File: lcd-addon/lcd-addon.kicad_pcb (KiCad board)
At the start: 2 copper layers, 39.4 x 26.9 mm, 8 parts, among them J1 Conn_01x02_Male, J2 Conn_01x07_Male, J4 Conn_01x10, J5 Conn_01x01_Male, J6 Conn_01x02_Male, J8 Conn_01x02_Male

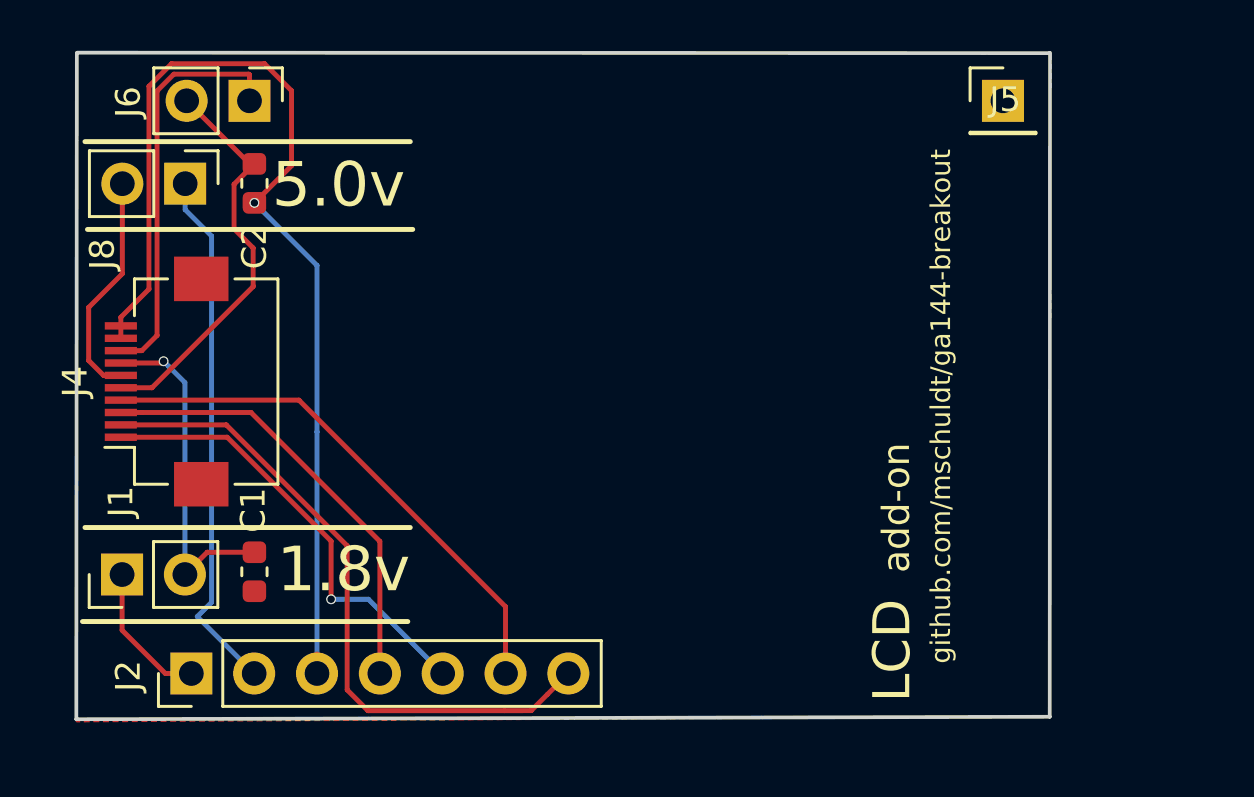
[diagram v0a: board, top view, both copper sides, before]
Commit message: lcd-addon: extend board length
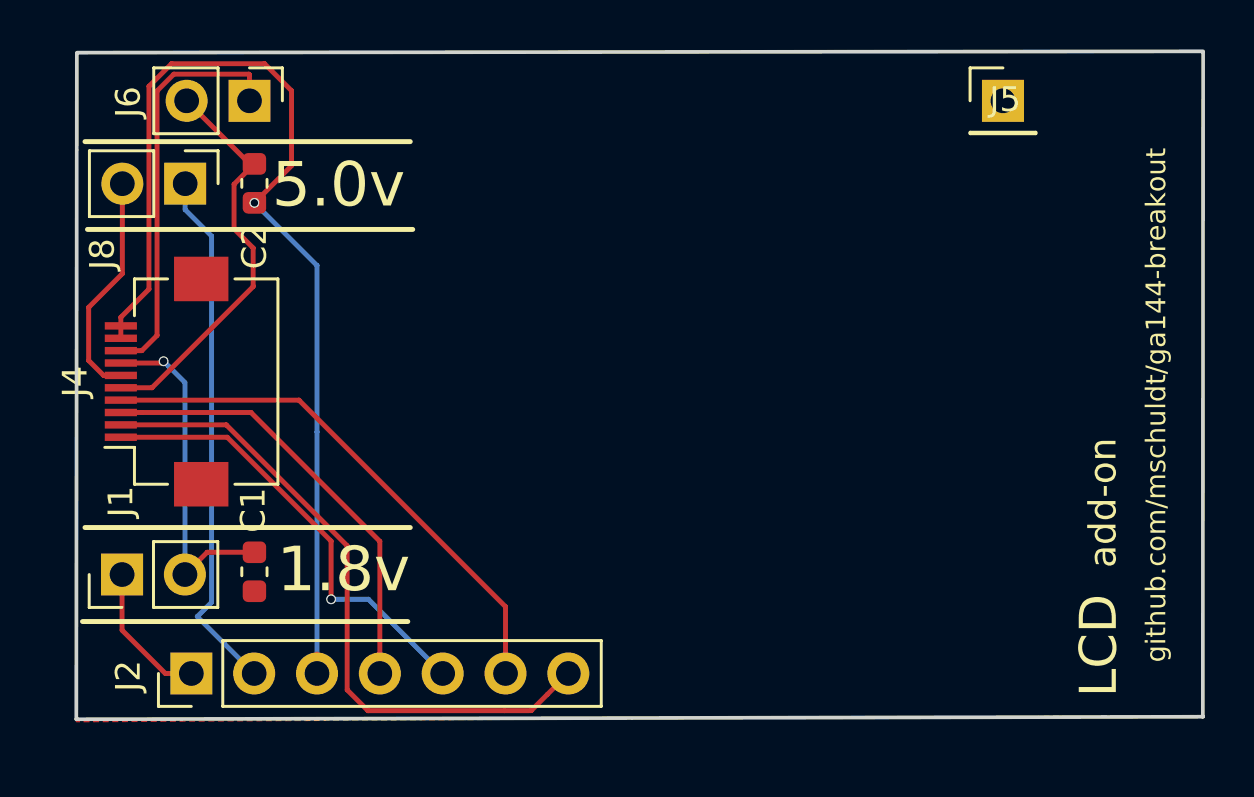
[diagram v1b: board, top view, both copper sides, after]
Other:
- board size 39.4 x 26.9 mm -> 45.5 x 27 mm
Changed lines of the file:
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@@
   )
   (setup
-    (last_trace_width 0.2)
+    (last_trace_width 0.127)
     (user_trace_width 0.127)
     (user_trace_width 0.16)
@@
     (effects (font (size 1.8 1.8) (thickness 0.3)))
   )
-  (gr_text add-on (at 140.55 91.65 90) (layer F.SilkS)
+  (gr_text add-on (at 148.9 91.45 90) (layer F.SilkS)
     (effects (font (size 1.1 1.1) (thickness 0.18)))
   )
-  (gr_text github.com/mschuldt/ga144-breakout (at 142.35 87.55 90) (layer F.SilkS)
+  (gr_text github.com/mschuldt/ga144-breakout (at 151.05 87.5 90) (layer F.SilkS)
     (effects (font (size 0.8 0.8) (thickness 0.15)))
   )
-  (gr_text LCD (at 140.3781 97.41884 90) (layer F.SilkS)
+  (gr_text LCD (at 148.7281 97.21884 90) (layer F.SilkS)
     (effects (font (size 1.5 1.5) (thickness 0.3)))
   )
-  (gr_line (start 146.73072 73.27392) (end 107.43184 73.2536) (layer Edge.Cuts) (width 0.15))
-  (gr_line (start 146.75 100.1) (end 146.7612 73.25868) (layer Edge.Cuts) (width 0.15))
-  (gr_line (start 107.4 100.2) (end 146.75 100.1) (layer Edge.Cuts) (width 0.15))
+  (gr_line (start 152.95 73.2) (end 107.43184 73.2536) (layer Edge.Cuts) (width 0.15))
+  (gr_line (start 152.9388 100.09132) (end 152.95 73.25) (layer Edge.Cuts) (width 0.15))
+  (gr_line (start 107.4 100.2) (end 152.95 100.1) (layer Edge.Cuts) (width 0.15))
   (gr_line (start 107.42168 73.27138) (end 107.4 100.2) (layer Edge.Cuts) (width 0.15))
   (segment (start 117.13 97.555) (end 117.13 98.35) (width 0.2) (layer F.Cu) (net 1))
@@
     (polygon
       (pts
-        (xy 107.45 73.25) (xy 146.8 73.3) (xy 146.75 100.1) (xy 107.4 100.3)
+        (xy 107.45 73.25) (xy 152.95 73.2) (xy 152.95 100.05) (xy 107.4 100.3)
       )
     )

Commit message: lcd-addon changes
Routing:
- net 008.5: track 18.3 -> 17.2 mm
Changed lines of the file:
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@@
-(kicad_pcb (version 20171130) (host pcbnew 5.0.1-33cea8e~68~ubuntu14.04.1)
+(kicad_pcb (version 20171130) (host pcbnew 5.0.2-bee76a0~70~ubuntu14.04.1)
   (general
     (thickness 1.6)
@@
   (segment (start 114.55 82.708602) (end 110.458602 86.8) (width 0.2) (layer F.Cu) (net 4))
   (segment (start 113.777001 80.377001) (end 114.55 81.15) (width 0.2) (layer F.Cu) (net 4))
-  (segment (start 119.67 93.007537) (end 114.462463 87.8) (width 0.2) (layer F.Cu) (net 5))
-  (segment (start 114.462463 87.8) (end 110.05 87.8) (width 0.2) (layer F.Cu) (net 5))
-  (segment (start 119.67 98.35) (end 119.67 93.007537) (width 0.2) (layer F.Cu) (net 5))
   (segment (start 110.05 87.8) (end 109.2 87.8) (width 0.2) (layer F.Cu) (net 5))
-  (segment (start 109.2 88.8) (end 113.5 88.8) (width 0.2) (layer F.Cu) (net 6))
-  (segment (start 117.7 93) (end 117.7 95.35) (width 0.2) (layer F.Cu) (net 6))
-  (via (at 117.7 95.35) (size 0.4) (drill 0.3) (layers F.Cu B.Cu) (net 6))
-  (segment (start 113.5 88.8) (end 117.7 93) (width 0.2) (layer F.Cu) (net 6))
-  (segment (start 119.21 95.35) (end 122.21 98.35) (width 0.2) (layer B.Cu) (net 6))
-  (segment (start 117.7 95.35) (end 119.21 95.35) (width 0.2) (layer B.Cu) (net 6))
+  (segment (start 114.978 87.8) (end 110.05 87.8) (width 0.2) (layer F.Cu) (net 5))
+  (segment (start 119.67 92.492) (end 114.978 87.8) (width 0.2) (layer F.Cu) (net 5))
+  (segment (start 119.67 98.35) (end 119.67 92.492) (width 0.2) (layer F.Cu) (net 5))
+  (via (at 117.7 93.472) (size 0.4) (drill 0.3) (layers F.Cu B.Cu) (net 6))
+  (segment (start 109.2 88.8) (end 113.028 88.8) (width 0.2) (layer F.Cu) (net 6))
+  (segment (start 113.028 88.8) (end 117.500001 93.272001) (width 0.2) (layer F.Cu) (net 6))
+  (segment (start 117.500001 93.272001) (end 117.7 93.472) (width 0.2) (layer F.Cu) (net 6))
+  (segment (start 117.7 93.57) (end 117.7 93.472) (width 0.2) (layer B.Cu) (net 6))
+  (segment (start 122.21 98.08) (end 117.7 93.57) (width 0.2) (layer B.Cu) (net 6))
+  (segment (start 122.21 98.35) (end 122.21 98.08) (width 0.2) (layer B.Cu) (net 6))
   (segment (start 124.75 98.35) (end 124.75 95.65) (width 0.2) (layer F.Cu) (net 7))
   (segment (start 116.4 87.3) (end 109.2 87.3) (width 0.2) (layer F.Cu) (net 7))
@@
   (segment (start 126.440001 99.199999) (end 127.29 98.35) (width 0.2) (layer F.Cu) (net 8))
   (segment (start 125.788742 99.851258) (end 126.440001 99.199999) (width 0.2) (layer F.Cu) (net 8))
+  (segment (start 124.708468 99.854003) (end 125.788742 99.851258) (width 0.2) (layer F.Cu) (net 8))
+  (segment (start 119.190001 99.854003) (end 124.708468 99.854003) (width 0.2) (layer F.Cu) (net 8))
+  (segment (start 118.35 92.696) (end 118.35 99.014002) (width 0.2) (layer F.Cu) (net 8))
   (segment (start 118.35 99.014002) (end 119.190001 99.854003) (width 0.2) (layer F.Cu) (net 8))
-  (segment (start 118.35 93.187538) (end 118.35 99.014002) (width 0.2) (layer F.Cu) (net 8))
-  (segment (start 124.708468 99.854003) (end 125.788742 99.851258) (width 0.2) (layer F.Cu) (net 8))
-  (segment (start 113.462462 88.3) (end 118.35 93.187538) (width 0.2) (layer F.Cu) (net 8))
-  (segment (start 119.190001 99.854003) (end 124.708468 99.854003) (width 0.2) (layer F.Cu) (net 8))
-  (segment (start 109.2 88.3) (end 113.462462 88.3) (width 0.2) (layer F.Cu) (net 8))
+  (segment (start 113.954 88.3) (end 118.35 92.696) (width 0.2) (layer F.Cu) (net 8))
+  (segment (start 109.2 88.3) (end 113.954 88.3) (width 0.2) (layer F.Cu) (net 8))
   (segment (start 112.69 93.45) (end 114.6 93.45) (width 0.2) (layer F.Cu) (net 9))
   (segment (start 111.79 94.35) (end 112.69 93.45) (width 0.2) (layer F.Cu) (net 9))
@@
   (segment (start 110.854718 85.8) (end 110.927359 85.727359) (width 0.2) (layer F.Cu) (net 9))
   (segment (start 111.79 86.59) (end 111.127358 85.927358) (width 0.2) (layer B.Cu) (net 9))
-  (segment (start 114.59 98.35) (end 112.29 96.05) (width 0.2) (layer B.Cu) (net 10))
+  (segment (start 112.867001 80.667001) (end 111.8 79.6) (width 0.2) (layer B.Cu) (net 10))
+  (segment (start 112.867001 96.627001) (end 112.867001 80.667001) (width 0.2) (layer B.Cu) (net 10))
   (segment (start 111.8 79.6) (end 111.8 78.55) (width 0.2) (layer B.Cu) (net 10))
-  (segment (start 112.867001 80.667001) (end 111.8 79.6) (width 0.2) (layer B.Cu) (net 10))
-  (segment (start 112.867001 95.472999) (end 112.867001 80.667001) (width 0.2) (layer B.Cu) (net 10))
-  (segment (start 112.29 96.05) (end 112.867001 95.472999) (width 0.2) (layer B.Cu) (net 10))
+  (segment (start 114.59 98.35) (end 112.867001 96.627001) (width 0.2) (layer B.Cu) (net 10))
   (segment (start 108.5 86.3) (end 109.2 86.3) (width 0.2) (layer F.Cu) (net 11))
   (segment (start 107.9 85.7) (end 108.5 86.3) (width 0.2) (layer F.Cu) (net 11))
